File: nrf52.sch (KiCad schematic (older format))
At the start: 5 parts, among them J11 NRFSWDCLK, J12 NRFSWDIO, J13 GND, U8 BMD-340-A-R

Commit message: tweaks
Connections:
- wire segments 31 -> 40
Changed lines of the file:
@@
 	1    0    0    -1
 $EndComp
-Text GLabel 7050 1800 2    50   Input ~ 0
+Text GLabel 6850 1150 1    50   Input ~ 0
 5V
-Text Notes 7250 1850 0    50   ~ 0
+Text Notes 5750 1850 0    50   ~ 0
 USB power\n
-Wire Wire Line
-	6450 1800 7050 1800
 $Comp
 L power:VCC #PWR048
@@
 $EndComp
 Wire Wire Line
-	6450 1600 6750 1600
+	6450 1600 6700 1600
 Wire Wire Line
 	6450 1700 6750 1700
@@
 Wire Wire Line
 	6450 4800 6850 4800
-Wire Wire Line
-	6850 4800 6850 4900
 Wire Wire Line
 	6450 4900 6850 4900
@@
 NoConn ~ 5350 3600
 NoConn ~ 5350 3500
-NoConn ~ 5350 3400
 NoConn ~ 5350 3300
 NoConn ~ 5350 3200
 NoConn ~ 5350 3100
 NoConn ~ 5350 3000
-NoConn ~ 6450 4100
-NoConn ~ 6450 4000
-NoConn ~ 6450 3900
-NoConn ~ 6450 3800
-NoConn ~ 6450 3700
-NoConn ~ 6450 3500
-NoConn ~ 6450 3400
-NoConn ~ 6450 3300
-NoConn ~ 6450 3200
-NoConn ~ 6450 3100
-NoConn ~ 6450 3000
-NoConn ~ 6450 2900
-NoConn ~ 6450 2800
-NoConn ~ 6450 2700
 NoConn ~ 5350 2900
 NoConn ~ 5350 2800
 NoConn ~ 5350 2700
-NoConn ~ 5350 2600
-NoConn ~ 6450 2600
-NoConn ~ 6450 2500
-NoConn ~ 6450 2400
-NoConn ~ 6450 2300
-NoConn ~ 6450 2200
-NoConn ~ 6450 2100
 NoConn ~ 5350 2400
 NoConn ~ 5350 2300
+Wire Wire Line
+	6450 1800 6850 1800
+Wire Wire Line
+	6850 1800 6850 1150
+$Comp
+L power:GND #PWR0103
+U 1 1 5CF9CBA9
+P 7400 1950
+F 0 "#PWR0103" H 7400 1700 50  0001 C CNN
+F 1 "GND" H 7405 1777 50  0000 C CNN
+F 2 "" H 7400 1950 50  0001 C CNN
+F 3 "" H 7400 1950 50  0001 C CNN
+	1    7400 1950
+	1    0    0    -1
+$EndComp
+Wire Wire Line
+	6950 1800 6950 1650
+Wire Wire Line
+	6950 1650 7400 1650
+Wire Wire Line
+	7400 1650 7400 1950
+Wire Wire Line
+	6950 1900 6700 1900
+Wire Wire Line
+	6700 1900 6700 1600
+Wire Wire Line
+	6700 1600 6750 1600
+Connection ~ 6700 1600
 NoConn ~ 6450 2000
+NoConn ~ 6450 2100
+NoConn ~ 6450 2200
+NoConn ~ 6450 2300
+NoConn ~ 6450 2400
+NoConn ~ 5350 2600
+NoConn ~ 5350 3400
+Wire Wire Line
+	6850 4800 6850 4900
+Wire Wire Line
+	7200 2200 6950 2200
+Wire Wire Line
+	6950 2200 6950 1900
+NoConn ~ 6450 2500
+NoConn ~ 6450 2600
+NoConn ~ 6450 2700
+NoConn ~ 6450 2800
+NoConn ~ 6450 2900
+NoConn ~ 6450 3000
+NoConn ~ 6450 3100
+NoConn ~ 6450 3200
+NoConn ~ 6450 3300
+NoConn ~ 6450 3400
+NoConn ~ 6450 3500
+NoConn ~ 6450 3700
+NoConn ~ 6450 3800
+NoConn ~ 6450 3900
+NoConn ~ 6450 4000
+NoConn ~ 6450 4100
 $EndSCHEMATC

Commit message: tweaks
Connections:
- wire segments 40 -> 32
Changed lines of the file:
@@
 $EndComp
-Wire Wire Line
-	6450 1600 6700 1600
 Wire Wire Line
 	6450 1700 6750 1700
@@
 Wire Wire Line
 	6850 1800 6850 1150
-$Comp
-L power:GND #PWR0103
-U 1 1 5CF9CBA9
-P 7400 1950
-F 0 "#PWR0103" H 7400 1700 50  0001 C CNN
-F 1 "GND" H 7405 1777 50  0000 C CNN
-F 2 "" H 7400 1950 50  0001 C CNN
-F 3 "" H 7400 1950 50  0001 C CNN
-	1    7400 1950
-	1    0    0    -1
-$EndComp
-Wire Wire Line
-	6950 1800 6950 1650
-Wire Wire Line
-	6950 1650 7400 1650
-Wire Wire Line
-	7400 1650 7400 1950
-Wire Wire Line
-	6950 1900 6700 1900
-Wire Wire Line
-	6700 1900 6700 1600
-Wire Wire Line
-	6700 1600 6750 1600
-Connection ~ 6700 1600
 NoConn ~ 6450 2000
 NoConn ~ 6450 2100
@@
 Wire Wire Line
 	6850 4800 6850 4900
-Wire Wire Line
-	7200 2200 6950 2200
-Wire Wire Line
-	6950 2200 6950 1900
 NoConn ~ 6450 2500
 NoConn ~ 6450 2600
@@
 NoConn ~ 6450 4000
 NoConn ~ 6450 4100
+Wire Wire Line
+	6450 1600 6750 1600
 $EndSCHEMATC

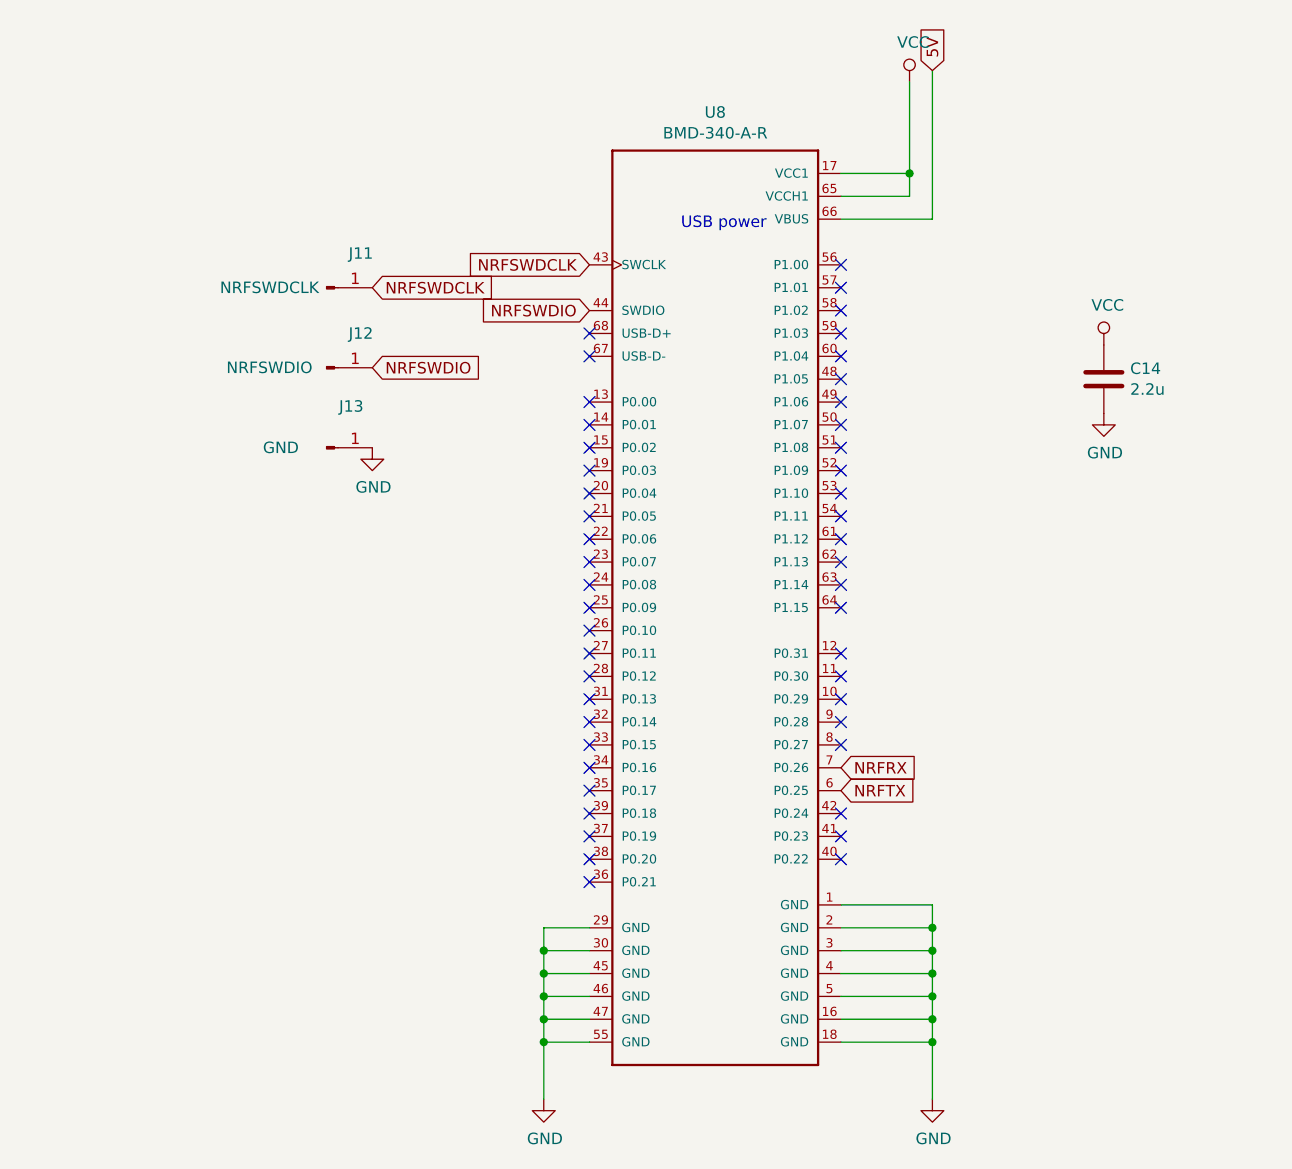
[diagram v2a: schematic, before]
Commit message: Routing done with nrf52
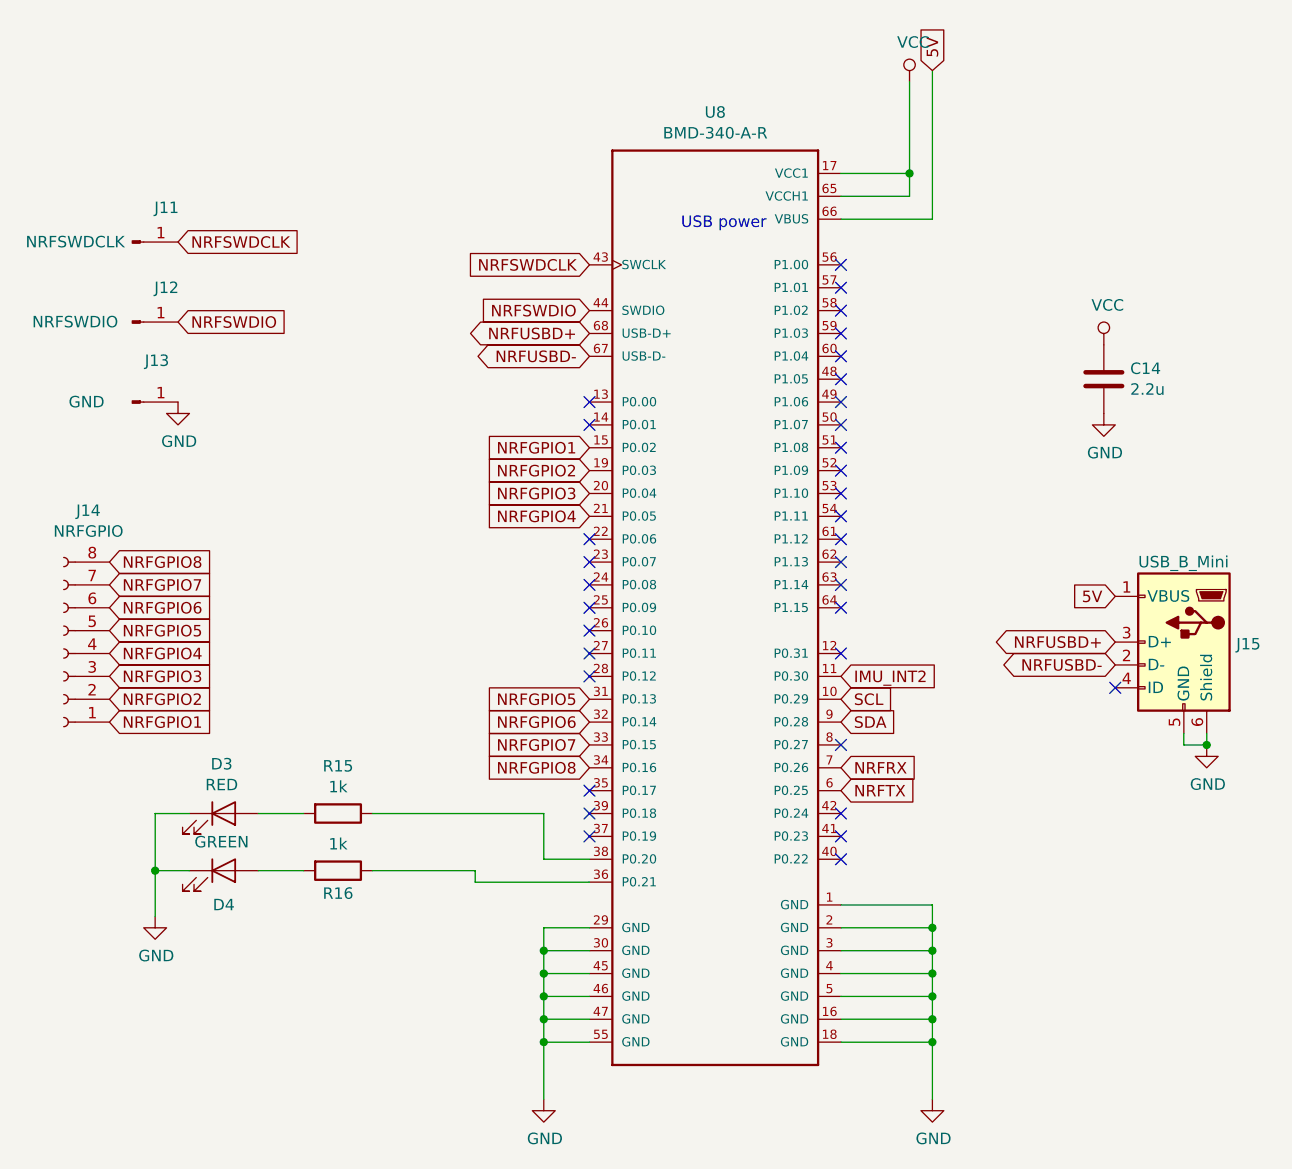
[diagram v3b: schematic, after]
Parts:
- added D3: RED, LED_SMD:LED_0603_1608Metric, symbol Device:LED
- added D4: GREEN, LED_SMD:LED_0603_1608Metric, symbol Device:LED
- added J14: NRFGPIO, Connector_JST:JST_PH_B8B-PH-K_1x08_P2.00mm_Vertical, symbol Connector:Conn_01x08_Female
- added J15: USB_B_Mini, Connector_USB:USB_Mini-B_Lumberg_2486_01_Horizontal, symbol Connector:USB_B_Mini
- added R15, R16: 1k, Resistor_SMD:R_0603_1608Metric, symbol Device:R
- J11, J12, J13: footprint TestPoint:TestPoint_Pad_2.5x2.5mm -> TestPoint:TestPoint_Pad_1.5x1.5mm
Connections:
- net 5V: now also J15.1 (VBUS)
- net GND: now also D3.1 (K), D4.1 (K), J15.5 (GND), J15.6 (Shield)
- net SCL: now reaches U8.10 (P0.29)
- net IMU_INT2: now reaches U8.11 (P0.30)
- net NRFGPIO1: now reaches U8.15 (P0.02)
- net NRFGPIO1: now also J14.1 (Pin_1)
- net NRFGPIO2: now reaches U8.19 (P0.03)
- net NRFGPIO2: now also J14.2 (Pin_2)
- net NRFGPIO3: now reaches U8.20 (P0.04)
- net NRFGPIO3: now also J14.3 (Pin_3)
- net NRFGPIO4: now reaches U8.21 (P0.05)
- net NRFGPIO4: now also J14.4 (Pin_4)
- net NRFGPIO5: now reaches U8.31 (P0.13)
- net NRFGPIO5: now also J14.5 (Pin_5)
- net NRFGPIO6: now reaches U8.32 (P0.14)
- net NRFGPIO6: now also J14.6 (Pin_6)
- net NRFGPIO7: now reaches U8.33 (P0.15)
- net NRFGPIO7: now also J14.7 (Pin_7)
- net NRFGPIO8: now reaches U8.34 (P0.16)
- net NRFGPIO8: now also J14.8 (Pin_8)
- net at U8.36 (P0.21): now also R16.1
- net at U8.38 (P0.20): now also R15.1
- net NRFUSBD-: now reaches U8.67 (USB-D-)
- net NRFUSBD-: now also J15.2 (D-)
- net NRFUSBD+: now reaches U8.68 (USB-D+)
- net NRFUSBD+: now also J15.3 (D+)
- net SDA: now reaches U8.9 (P0.28)
- new net: D4.2 (A), R16.2
- new net: D3.2 (A), R15.2
- no-connect marks 48 -> 34
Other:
- moved on the sheet: J11, J12, J13
